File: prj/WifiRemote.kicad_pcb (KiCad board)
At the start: 2 copper layers, 40 x 75 mm, 70 parts, among them J1 2AA_Battery, J2 DIP-BLACK-MALE-HEADER_6P-2.54_, K1 DIP-SWITCH-TACTILE-SPST-NO_TS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, K2 DIP-SWITCH-TACTILE-SPST-NO_TS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, K3 DIP-SWITCH-TACTILE-SPST-NO_TS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, K4 DIP-SWITCH-TACTILE-SPST-NO_TS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, M1 Mechanical_Mount, M2 Mechanical_Mount, M3 Mechanical_Mount, M4 Mechanical_Mount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

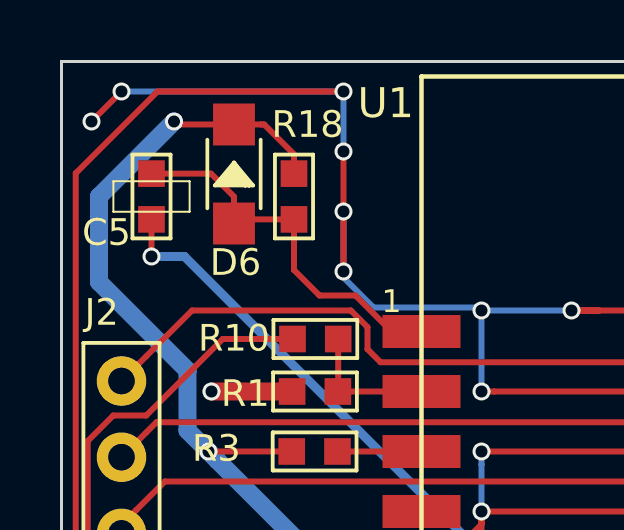
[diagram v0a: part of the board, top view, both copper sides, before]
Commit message: Changed R6 and R8 to 330R and added C10
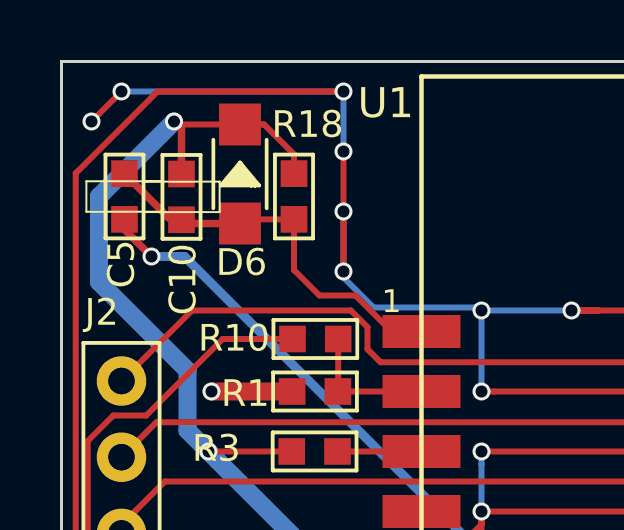
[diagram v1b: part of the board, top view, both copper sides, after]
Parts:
- added C10: CERAMIC-100NF-50V-10%-X7R_0603_, SeeedOPL-Capacitor-2016:C0603, F.Cu at (54.0, 79.5)
- R6, R8: value SMD-RES-10R-5%-1_10W_0603_ -> SMD-RES-330R-1%-1_10W_0603_
- moved C5 0.90 mm to (52.1, 79.5)
- moved D6 0.20 mm to (56.0, 78.8)
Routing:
- net +3V3: track 117.1 -> 118.9 mm
- net RST: track 12.8 -> 13.4 mm
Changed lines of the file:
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@@
 (kicad_pcb (version 4) (host pcbnew 4.0.2+dfsg1-stable)
   (general
-    (links 127)
+    (links 129)
     (no_connects 0)
-    (area 39.321033 63.026366 102.202967 165.694)
+    (area 49.949999 74.949999 90.050001 150.050001)
     (thickness 1.6)
     (drawings 20)
-    (tracks 538)
+    (tracks 541)
     (zones 0)
-    (modules 70)
+    (modules 71)
     (nets 48)
   )
@@
   )
   (module SeeedOPL-Capacitor-2016:C0603 (layer F.Cu)
-    (at 53 79.5)
+    (at 52.1 79.5)
     (descr 0603)
     (tags 0603)
     (attr smd)
-    (fp_text reference C5 (at -1.5 1.2) (layer F.SilkS)
+    (fp_text reference C5 (at -0.1 2.25 90) (layer F.SilkS)
       (effects (font (size 0.889 0.889) (thickness 0.1016)))
     )
@@
       (effects (font (size 0.889 0.889) (thickness 0.1016)))
     )
-    (fp_text value SMD-RES-10R-5%-1_10W_0603_ (at 1.11506 -0.29972 360) (layer F.SilkS) hide
+    (fp_text value SMD-RES-330R-1%-1_10W_0603_ (at 1.11506 -0.29972 360) (layer F.SilkS) hide
       (effects (font (size 0.635 0.635) (thickness 0.0762)))
     )
@@
       (effects (font (size 0.889 0.889) (thickness 0.1016)))
     )
-    (fp_text value SMD-RES-10R-5%-1_10W_0603_ (at 1.11506 -0.29972 360) (layer F.SilkS) hide
+    (fp_text value SMD-RES-330R-1%-1_10W_0603_ (at 1.11506 -0.29972 360) (layer F.SilkS) hide
       (effects (font (size 0.635 0.635) (thickness 0.0762)))
     )
@@
   )
   (module SeeedOPL-Diode-2016:SOD-123 (layer F.Cu)
-    (at 55.75 78.75 90)
+    (at 55.95 78.75 90)
     (descr DIODE)
     (tags DIODE)
@@
       (xy -3.405671 -2.977842) (xy -3.360791 -2.974304)) (layer F.SilkS) (width 0.01))
   )
+  (module SeeedOPL-Capacitor-2016:C0603 (layer F.Cu)
+    (at 54 79.512)
+    (descr 0603)
+    (tags 0603)
+    (attr smd)
+    (fp_text reference C10 (at 0.05 2.75 270) (layer F.SilkS)
+      (effects (font (size 0.889 0.889) (thickness 0.1016)))
+    )
+    (fp_text value CERAMIC-100NF-50V-10%-X7R_0603_ (at -1.27 0.635 90) (layer F.SilkS) hide
+      (effects (font (size 0.635 0.635) (thickness 0.0762)))
+    )
+    (fp_line (start -1.27 0.508) (end 1.27 0.508) (layer F.SilkS) (width 0.06604))
+    (fp_line (start 1.27 0.508) (end 1.27 -0.508) (layer F.SilkS) (width 0.06604))
+    (fp_line (start -1.27 -0.508) (end 1.27 -0.508) (layer F.SilkS) (width 0.06604))
+    (fp_line (start -1.27 0.508) (end -1.27 -0.508) (layer F.SilkS) (width 0.06604))
+    (fp_line (start 0.635 -1.397) (end 0.635 1.397) (layer F.SilkS) (width 0.127))
+    (fp_line (start 0.635 1.397) (end -0.635 1.397) (layer F.SilkS) (width 0.127))
+    (fp_line (start -0.635 1.397) (end -0.635 -1.397) (layer F.SilkS) (width 0.127))
+    (fp_line (start -0.635 -1.397) (end 0.635 -1.397) (layer F.SilkS) (width 0.127))
+    (pad 1 smd rect (at 0 -0.762 270) (size 0.889 0.889) (layers F.Cu F.Paste F.Mask)
+      (net 8 +3V3))
+    (pad 2 smd rect (at 0 0.762 270) (size 0.889 0.889) (layers F.Cu F.Paste F.Mask)
+      (net 1 RST))
+  )
   (gr_text 09/24/2017 (at 65.2 142.1) (layer F.SilkS)
     (effects (font (size 0.75 0.75) (thickness 0.1875)))
@@
   (gr_line (start 90 150) (end 90 75) (layer Edge.Cuts) (width 0.1))
   (gr_line (start 50 150) (end 90 150) (layer Edge.Cuts) (width 0.1))
+  (segment (start 54 80.212) (end 53.574 80.212) (width 0.25) (layer F.Cu) (net 1))
+  (segment (start 53.574 80.212) (end 52.1 78.738) (width 0.25) (layer F.Cu) (net 1))
+  (segment (start 55.95 80.401) (end 54.189 80.401) (width 0.25) (layer F.Cu) (net 1))
+  (segment (start 54.189 80.401) (end 54 80.212) (width 0.25) (layer F.Cu) (net 1))
   (segment (start 57.75 80.262) (end 57.75 81.95) (width 0.2) (layer F.Cu) (net 1))
   (segment (start 57.75 81.95) (end 58.6 82.8) (width 0.2) (layer F.Cu) (net 1))
@@
   (segment (start 59.8 82.8) (end 61 84) (width 0.2) (layer F.Cu) (net 1))
   (segment (start 61 84) (end 62 84) (width 0.2) (layer F.Cu) (net 1))
-  (segment (start 55.75 80.401) (end 55.75 79.5025) (width 0.2) (layer F.Cu) (net 1))
-  (segment (start 55.75 79.5025) (end 54.9855 78.738) (width 0.2) (layer F.Cu) (net 1))
-  (segment (start 54.9855 78.738) (end 53.6445 78.738) (width 0.2) (layer F.Cu) (net 1))
-  (segment (start 53.6445 78.738) (end 53 78.738) (width 0.2) (layer F.Cu) (net 1))
   (segment (start 57.75 80.262) (end 55.889 80.262) (width 0.2) (layer F.Cu) (net 1))
   (segment (start 55.889 80.262) (end 55.75 80.401) (width 0.2) (layer F.Cu) (net 1))
+  (segment (start 52.1 80.262) (end 52.1 80.6) (width 0.25) (layer F.Cu) (net 2))
+  (segment (start 52.1 80.6) (end 53 81.5) (width 0.25) (layer F.Cu) (net 2))
   (segment (start 53 81.5) (end 54.1 81.5) (width 0.3) (layer B.Cu) (net 2))
   (segment (start 54.1 81.5) (end 64.6 92) (width 0.3) (layer B.Cu) (net 2))
   (segment (start 64.6 92) (end 75.575736 92) (width 0.3) (layer B.Cu) (net 2))
   (segment (start 75.575736 92) (end 76 92) (width 0.3) (layer B.Cu) (net 2))
-  (segment (start 53 80.262) (end 53 81.5) (width 0.2) (layer F.Cu) (net 2))
   (via (at 53 81.5) (size 0.6) (drill 0.4) (layers F.Cu B.Cu) (net 2))
   (segment (start 78 92) (end 76 92) (width 0.2) (layer F.Cu) (net 2))
@@
   (segment (start 87.889 90) (end 87.889 91.873) (width 0.2) (layer F.Cu) (net 7))
   (segment (start 87.889 91.873) (end 87.762 92) (width 0.2) (layer F.Cu) (net 7))
+  (segment (start 54 78.688) (end 54 77.25) (width 0.25) (layer F.Cu) (net 8))
+  (segment (start 54 77.25) (end 53.75 77) (width 0.25) (layer F.Cu) (net 8))
   (segment (start 83.09999 94) (end 82.09999 93) (width 0.6) (layer B.Cu) (net 8))
   (segment (start 82.09999 93) (end 61 93) (width 0.6) (layer B.Cu) (net 8))

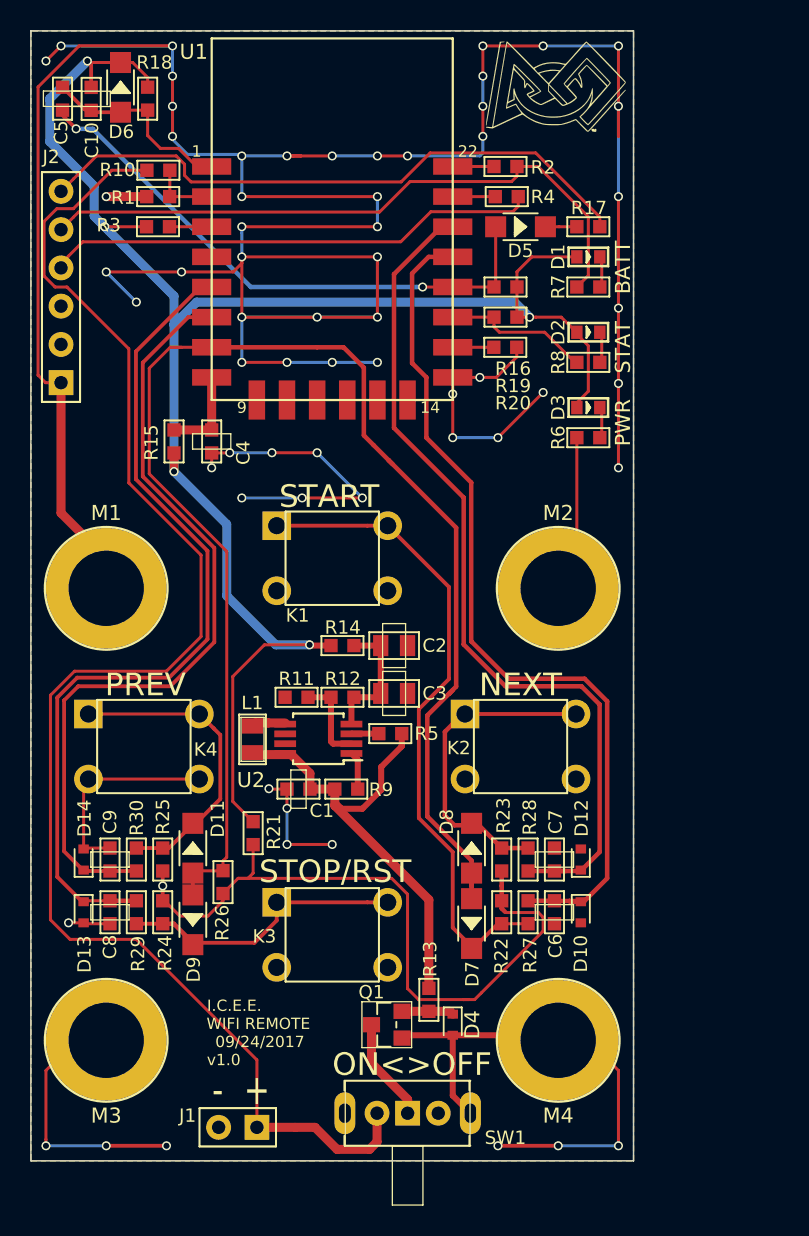
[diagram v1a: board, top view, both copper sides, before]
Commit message: Updated silk screen issue and changed inductor footprint
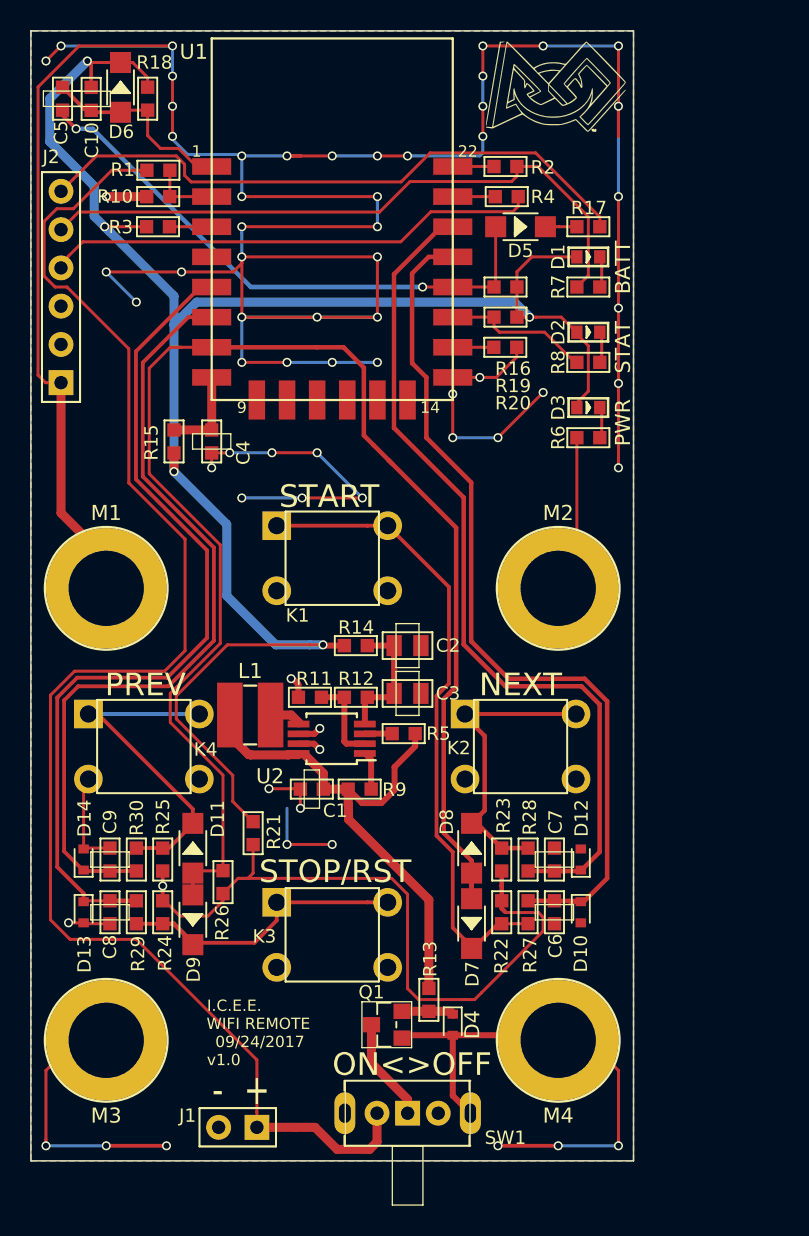
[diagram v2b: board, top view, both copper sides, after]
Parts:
- L1: footprint SeeedOPL-Inductor-2016:L0805 -> ICEE-Inductor:ICEE_Inductor_SPD3D16-4R7M
- moved L1 1.62 mm to (64.6, 120.4), turned to 0 degrees
- moved R5 0.89 mm to (74.7, 121.6)
- moved C1 0.89 mm to (68.6, 125.3)
- moved C2 0.89 mm to (75.0, 115.8)
- moved C3 0.89 mm to (75.0, 119.0)
- moved R11 0.89 mm to (68.5, 119.2)
- moved R12 0.89 mm to (71.6, 119.2)
- moved R14 0.89 mm to (71.6, 115.8)
- moved R9 0.89 mm to (71.8, 125.3)
- moved U2 0.89 mm to (70.0, 122.0)
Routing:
- net GNDD: track 342.2 -> 335.0 mm, vias 62 -> 63
- net +3V3: track 118.9 -> 125.2 mm
- net (no net): track 0.00 -> 5.40 mm, vias 0 -> 2
- net /REG_IN: track 31.8 -> 34.5 mm
- net /SW4: track 20.5 -> 22.4 mm
- net GPIO13: track 97.1 -> 98.8 mm
- net /SW1: track 43.4 -> 42.4 mm
- net +BATT: track 99.8 -> 98.8 mm
- net /SW2: track 21.4 -> 20.5 mm

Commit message: Replaced TVS Diode footprint to included polarity marker
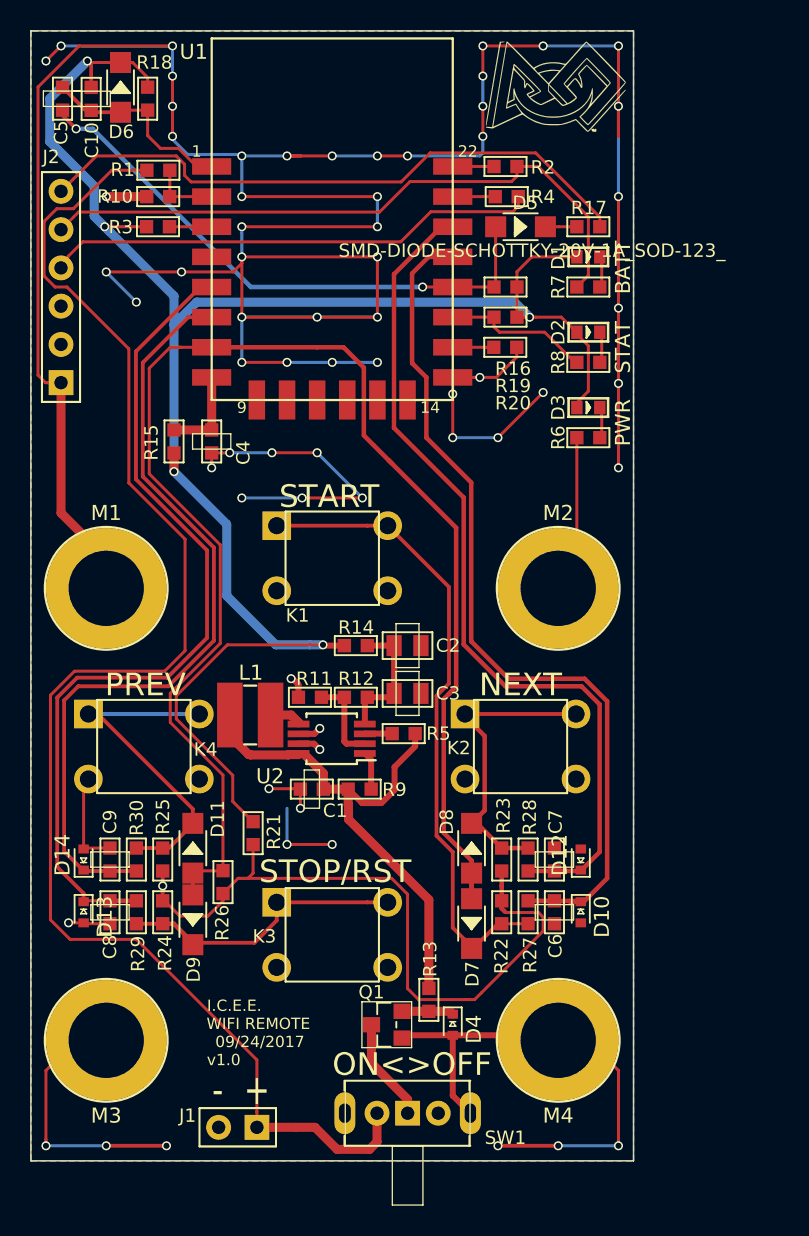
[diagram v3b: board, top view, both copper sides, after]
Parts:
- D10, D12, D13, D14, D4: footprint ICEE-Diode:SOD-523 -> ICEE-Diode:SOD-523_IMPROVED
